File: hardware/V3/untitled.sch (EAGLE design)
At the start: 27 parts, among them U1 ADAFRUIT_MPL3115A2_BAROMETER, U2 ADAFRUIT_MTK3339_GPS, U4 SPARKFUN_MPU9250_IMU, U5 RFM95W-915S2

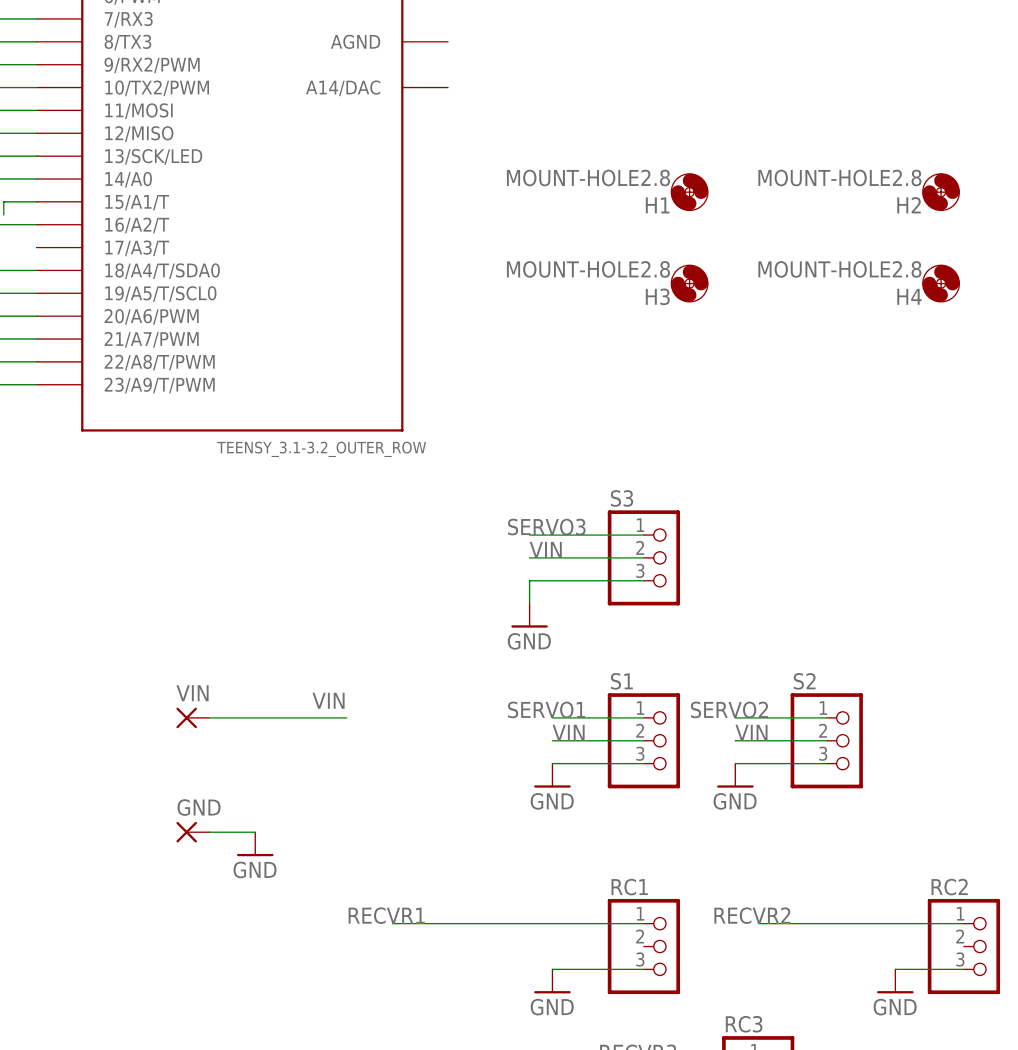
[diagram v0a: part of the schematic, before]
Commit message: added screw terminal to board; combined filter with imu scope
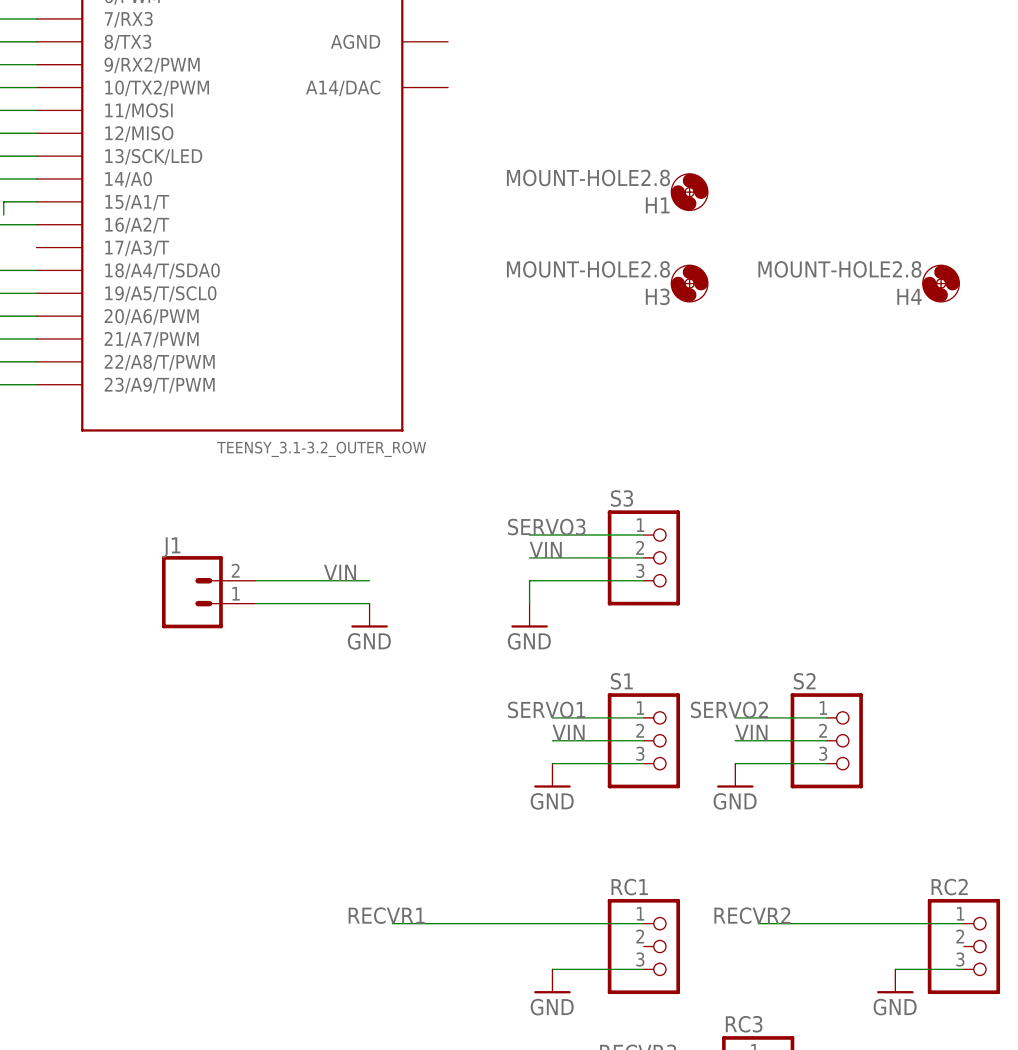
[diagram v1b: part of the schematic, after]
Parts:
- removed GND, VIN: (no value), wirepad:2,54/0,9
- removed H2: MOUNT-HOLE2.8, holes:MOUNT-HOLE2.8
- added J1: (no value), SparkFun-Connectors:CONN_025MM
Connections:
- net GND: now also J1.1; no longer GND.P
- net VIN: now also J1.2; no longer VIN.P
